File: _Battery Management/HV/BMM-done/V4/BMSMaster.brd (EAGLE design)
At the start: 83.8 x 91.4 mm, 119 parts, among them J1 M2_DF13-2P, J10 IMD, J14 USB_B_RA, J2 M2_DF13-2P, J3 M8S08B-PASK-2(LF)(SN), J5 M16_M_194280016, J6 M2770166, J7 M2770166, J8 M2770166, J9 M2770166, K1 ADJ14024, Q1 IRFR9120TRPBF, Q3 BSS123, U1 SN75HVD08DRMSOP, U10 NC7S14M5X, U11 LTC6820, U12 FT24C64A, U2 NCP1117DT_3.3, U22 NCV7805BDTRKG, U23 NUD3160DMT1G, U3 FT230X, U4 SN74LVC2G241, U5 NC7S14M5X, U6 DSPIC33FJ128GP804, U7 DMG6602SVTQ, U8 LTC6820, U9 MAX823TEUK+T_3.08, Y1 12Mhz

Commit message: Reroute
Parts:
- moved R3 36.9 mm to (77.3, 81.0), flipped to the top
- moved R16 3.45 mm to (35.9, 78.8)
- moved C2 3.32 mm to (33.8, 78.8), turned to 270 degrees
- moved U$1 2.51 mm to (75.6, 81.8), turned to 0 degrees
- moved C1 1.89 mm to (48.9, 72.0)
- moved C18 1.41 mm to (42.9, 73.7)
- moved C19 1.31 mm to (51.2, 74.9)
- moved J11 1.14 mm to (59.2, 82.7)
- moved R29 1.14 mm to (61.8, 78.9)
- moved R30 1.14 mm to (64.2, 78.9)
- moved R31 1.14 mm to (59.3, 78.9)
- moved J12 0.58 mm to (56.1, 91.4)
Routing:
- net SDA: track 68.8 -> 33.5 mm, vias 4 -> 1
- net SCL: track 74.1 -> 39.5 mm, vias 4 -> 1
- net EN1: track 3.93 -> 35.8 mm, vias 0 -> 2
- net +3V3: track 22.9 -> 50.0 mm, vias 1 -> 4
- net CS1: track 4.34 -> 30.0 mm, vias 0 -> 2
- net N$46: track 0.00 -> 6.47 mm, vias 0 -> 1
- net N$45: track 7.06 -> 9.55 mm

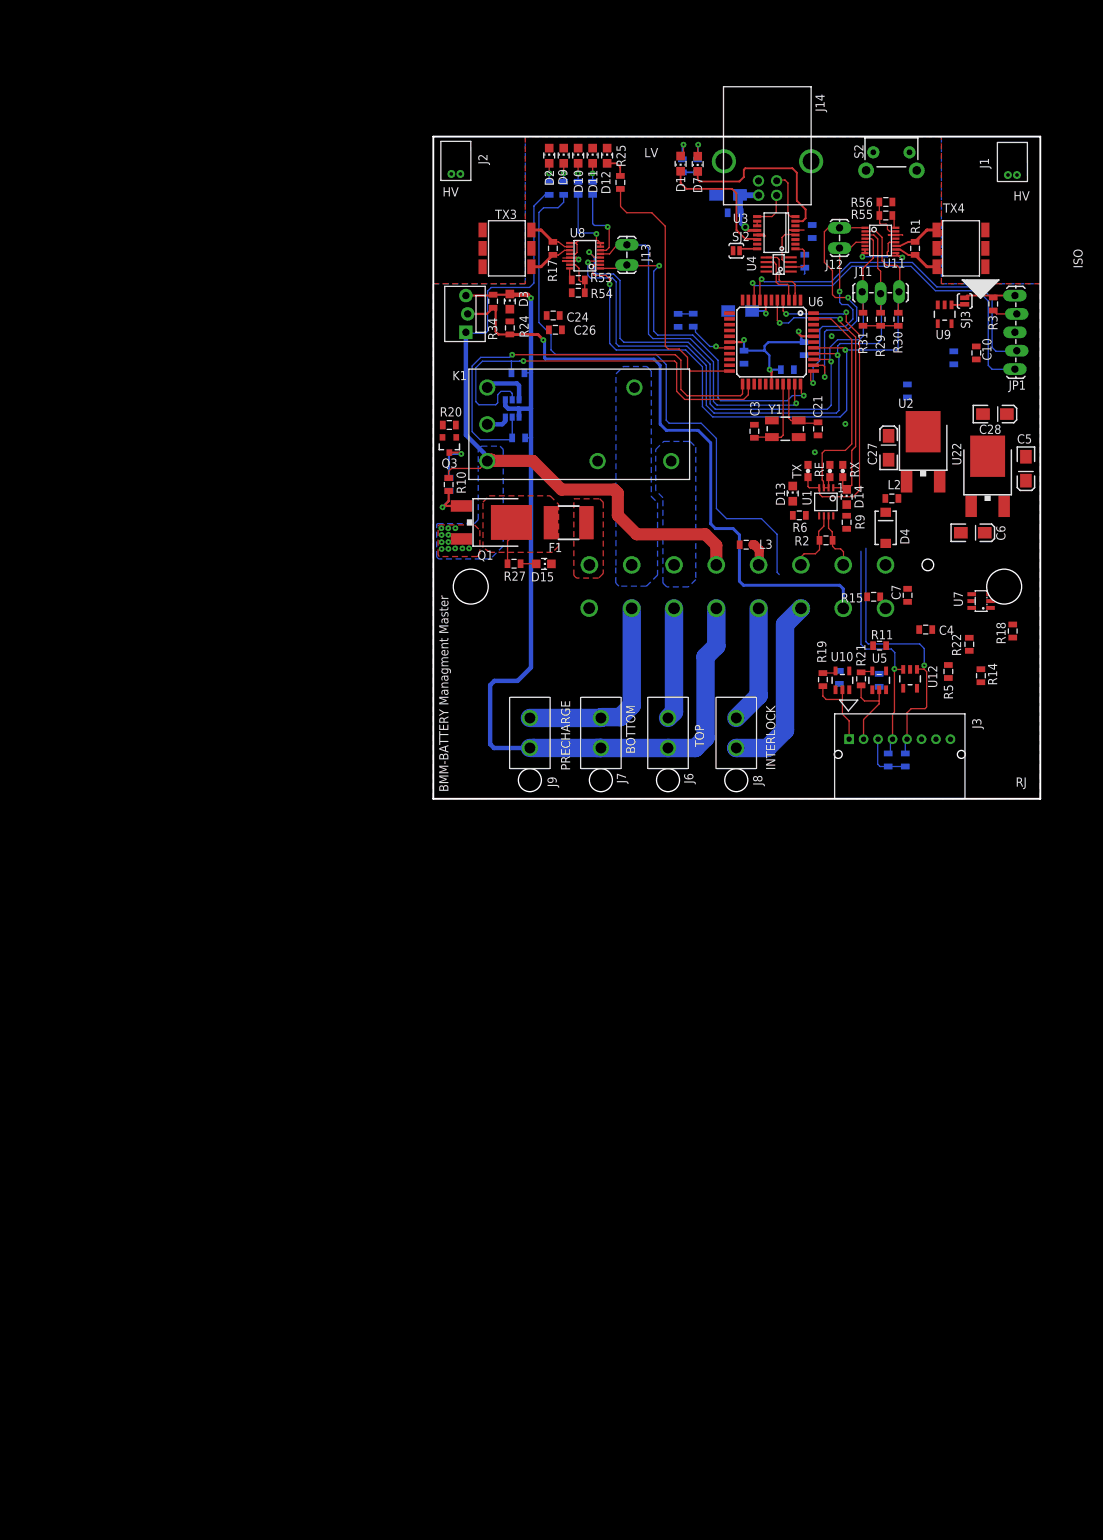
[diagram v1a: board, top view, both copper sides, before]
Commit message: Routing/ changing power supply
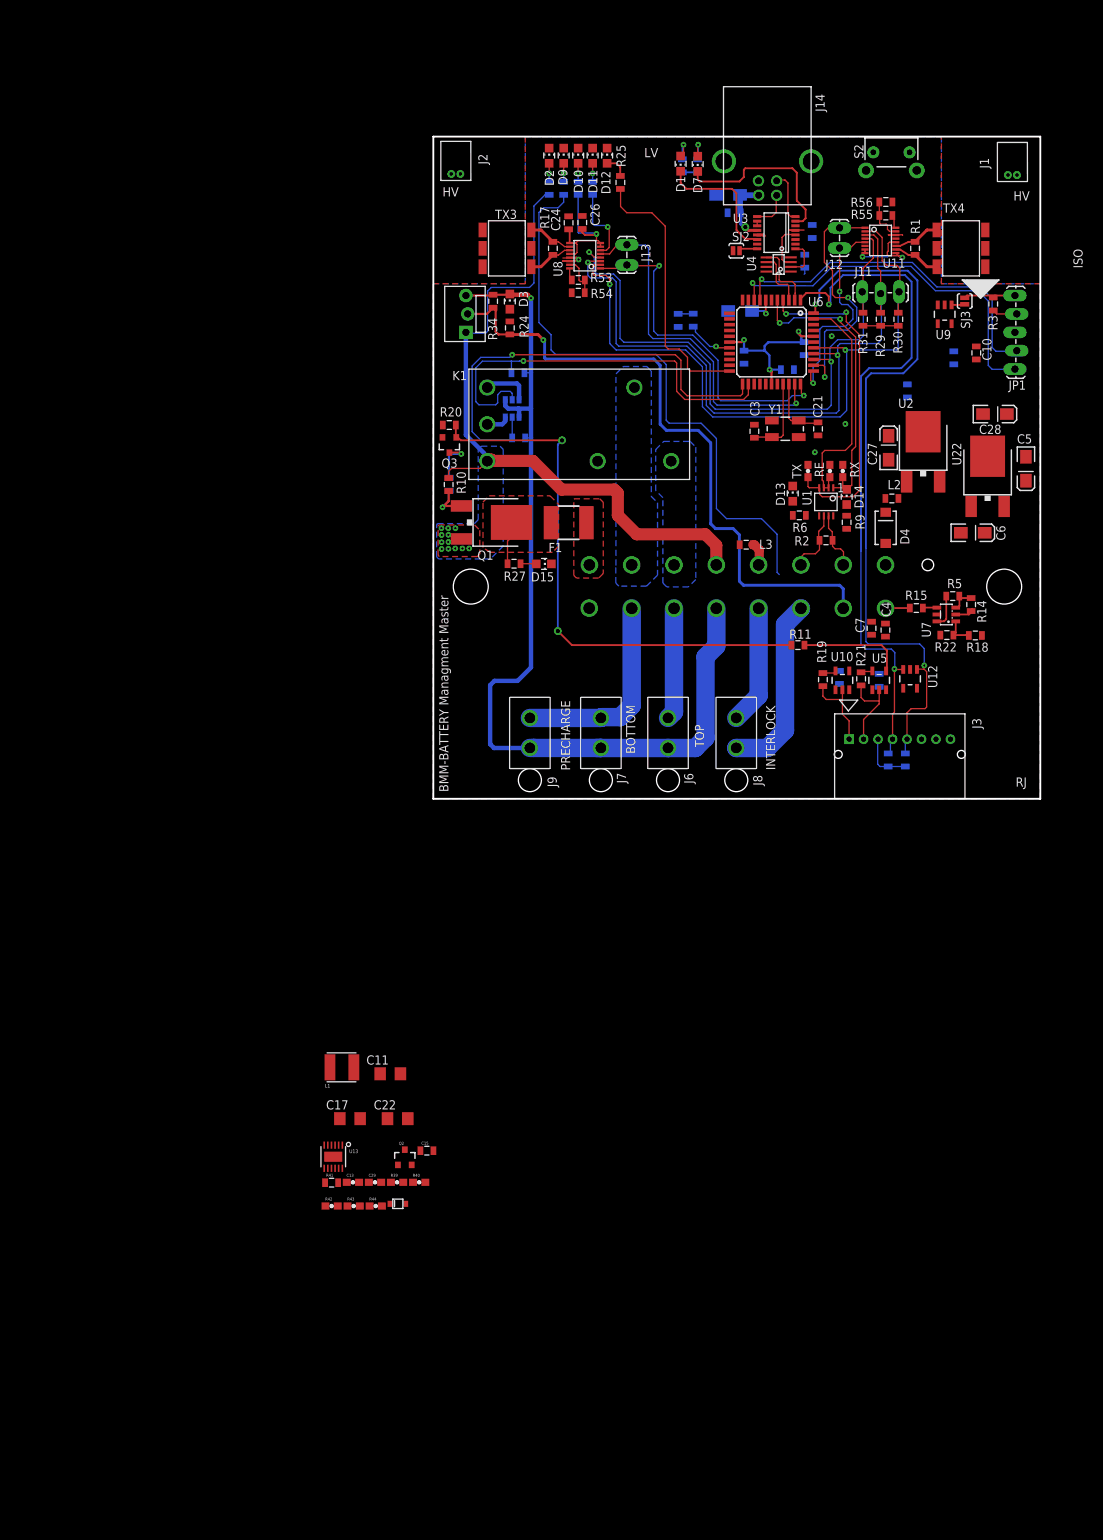
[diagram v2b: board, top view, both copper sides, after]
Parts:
- added C11: 4.7uF, FSAE Electric:1206@1
- added C13: 0.1uF, FSAE Electric:0603
- added C15: 1uF, FSAE Electric:0805
- added C17, C22: 10uF, FSAE Electric:1206@1
- added C29: 100pF, FSAE Electric:0603
- added D5: 22V, FSAE Electric:SOD-323
- added L1: SRN4018-220M, FSAE Electric:SRN4018
- added Q2: 40V 0.2A, FSAE Electric:SOT23
- added R39, R40, R44: 10k, FSAE Electric:0603
- added R41: 91k, FSAE Electric:0805
- added R42: 47k, FSAE Electric:0603
- added R43: 12.4k, FSAE Electric:0603
- added U13: ISL85415-FRZ-T7A, FSAE Electric:DFN-12
- moved C26 15.3 mm to (20.6, 92.3), turned to 90 degrees
- moved C24 13.0 mm to (18.7, 92.2), turned to 90 degrees
- moved R11 11.3 mm to (50.3, 33.9)
- moved R5 10.4 mm to (71.7, 40.7), turned to 0 degrees
- moved R14 9.92 mm to (74.3, 39.5)
- moved C7 6.74 mm to (60.5, 36.2)
- moved R15 6.09 mm to (66.7, 39.0), turned to 0 degrees
- moved C4 5.56 mm to (62.4, 36.0), turned to 270 degrees
- moved R18 5.19 mm to (74.9, 35.3), turned to 180 degrees
- moved U7 5.15 mm to (70.8, 38.2)
- moved R22 3.35 mm to (70.9, 35.3), turned to 0 degrees
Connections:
- new net N$21: D5.P$2, R40.2, R44.1
- new net N$52: Q2.2, R42.2, U13.7
- new net N$53: D5.P$1, R39.1
- new net N$55: C13.1, L1.P$1, U13.5
- new net N$56: C13.2, U13.3
- new net N$57: C15.1, U13.1, U13.11, U13.12, U13.9
- new net N$58: Q2.1, R44.2
- new net N$59: C11.1, Q2.3, R39.2, U13.4
- new net N$66: C29.2, R41.1, R43.2, U13.10
- net +5V: now also C17.1, C22.1, C29.1, L1.P$2, R41.2
- net GND: now also C11.2, C15.2, C17.2, C22.2, R40.1, R42.1, R43.1, U13.13, U13.2, U13.6
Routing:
- net TSAL_EN: track 0.00 -> 76.2 mm, vias 0 -> 2
- net SDA: track 33.5 -> 96.7 mm, vias 1 -> 2
- net SCL: track 39.5 -> 100.9 mm, vias 1 -> 2
- net N$19: track 0.00 -> 15.2 mm
- net +5V: track 32.9 -> 37.5 mm
- net N$40: track 0.00 -> 4.60 mm
- net TSAL_EN1: track 0.00 -> 4.19 mm
- net N$39: track 0.00 -> 3.65 mm
- net CS_OUT: track 0.00 -> 3.59 mm
- net +9V: track 82.3 -> 85.5 mm
- net N$49: track 0.00 -> 1.97 mm

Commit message: Trying to figure out DC/DC converter
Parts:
- removed C11: 4.7uF, FSAE Electric:1206@1
- removed C13: 0.1uF, FSAE Electric:0603
- removed C15: 1uF, FSAE Electric:0805
- removed C17, C22: 10uF, FSAE Electric:1206@1
- removed C27, C28, C5, C6: 10UF, FSAE Electric:EIA3216-16V
- removed C29: 100pF, FSAE Electric:0603
- removed D5: 22V, FSAE Electric:SOD-323
- removed L1: SRN4018-220M, FSAE Electric:SRN4018
- removed Q2: 40V 0.2A, FSAE Electric:SOT23
- removed R39, R40, R44: 10k, FSAE Electric:0603
- removed R41: 91k, FSAE Electric:0805
- removed R42: 47k, FSAE Electric:0603
- removed R43: 12.4k, FSAE Electric:0603
- removed U13: ISL85415-FRZ-T7A, FSAE Electric:DFN-12
- removed U2: NCP1117DT_3.3, FSAE Electric:DPAK
- removed U22: NCV7805BDTRKG, FSAE Electric:DPAK
- moved R34 61.3 mm to (8.20, 20.1), flipped to the bottom, turned to 90 degrees
- moved J10 58.4 mm to (5.36, 21.3), turned to 270 degrees
- moved JP1 37.3 mm to (57.6, 101.7), turned to 180 degrees
- moved R3 33.7 mm to (48.6, 98.7), turned to 0 degrees
- moved U$1 31.6 mm to (47.8, 96.9), turned to 90 degrees
- moved C10 29.5 mm to (55.3, 96.3), turned to 0 degrees
- moved SJ3 28.5 mm to (48.2, 94.7), turned to 180 degrees
- moved C25 25.0 mm to (56.5, 93.3), turned to 180 degrees
- moved U9 24.0 mm to (50.0, 91.9), turned to 270 degrees
- moved D1 20.1 mm to (24.4, 118.0)
- moved R7 20.1 mm to (24.6, 117.7)
- moved D7 20.1 mm to (26.8, 118.0)
- moved R8 20.1 mm to (26.7, 117.7)
- moved R24 19.6 mm to (13.8, 97.0)
- moved D3 19.5 mm to (13.8, 100.6)
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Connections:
- removed net N$21: D5.P$2, R40.2, R44.1
- removed net N$52: Q2.2, R42.2, U13.7
- removed net N$53: D5.P$1, R39.1
- removed net N$55: C13.1, L1.P$1, U13.5
- removed net N$56: C13.2, U13.3
- removed net N$57: C15.1, U13.1, U13.11, U13.12, U13.9
- removed net N$58: Q2.1, R44.2
- removed net N$59: C11.1, Q2.3, R39.2, U13.4
- removed net N$66: C29.2, R41.1, R43.2, U13.10
- new net N$60: L3.1
- net +3V3: no longer C28.A, U2.2
- net +5V: no longer C17.1, C22.1, C27.A, C29.1, L1.P$2, R41.2, U22.3
- net +9V: no longer C5.A, C6.A, U2.3, U22.1
- net GND: no longer C11.2, C15.2, C17.2, C22.2, C27.C, C28.C, C5.C, C6.C, L3.1, R40.1, R42.1, R43.1, U13.13, U13.2, U13.6, U2.1, U22.2
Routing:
- net N$48: track 51.0 -> 0.00 mm, vias 1 -> 0
- net N$47: track 48.5 -> 0.00 mm, vias 1 -> 0
- net VSS: track 132.8 -> 167.7 mm, vias 1 -> 2
- net IMD: track 89.1 -> 123.7 mm, vias 1 -> 4
- net +24V: track 94.7 -> 125.0 mm
- net N$44: track 37.5 -> 11.2 mm
- net N$8: track 24.9 -> 0.00 mm
- net N$10: track 18.4 -> 0.00 mm
- net USB_RX: track 9.41 -> 0.00 mm
- net USB_TX: track 7.87 -> 0.00 mm
- net N$1: track 3.27 -> 0.00 mm
- net +9V: track 85.5 -> 83.0 mm
- net N$42: track 0.00 -> 1.64 mm
- net N$69: track 0.93 -> 0.00 mm
- net N$30: track 2.55 -> 3.38 mm
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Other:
- outline, holes or cut-outs redrawn

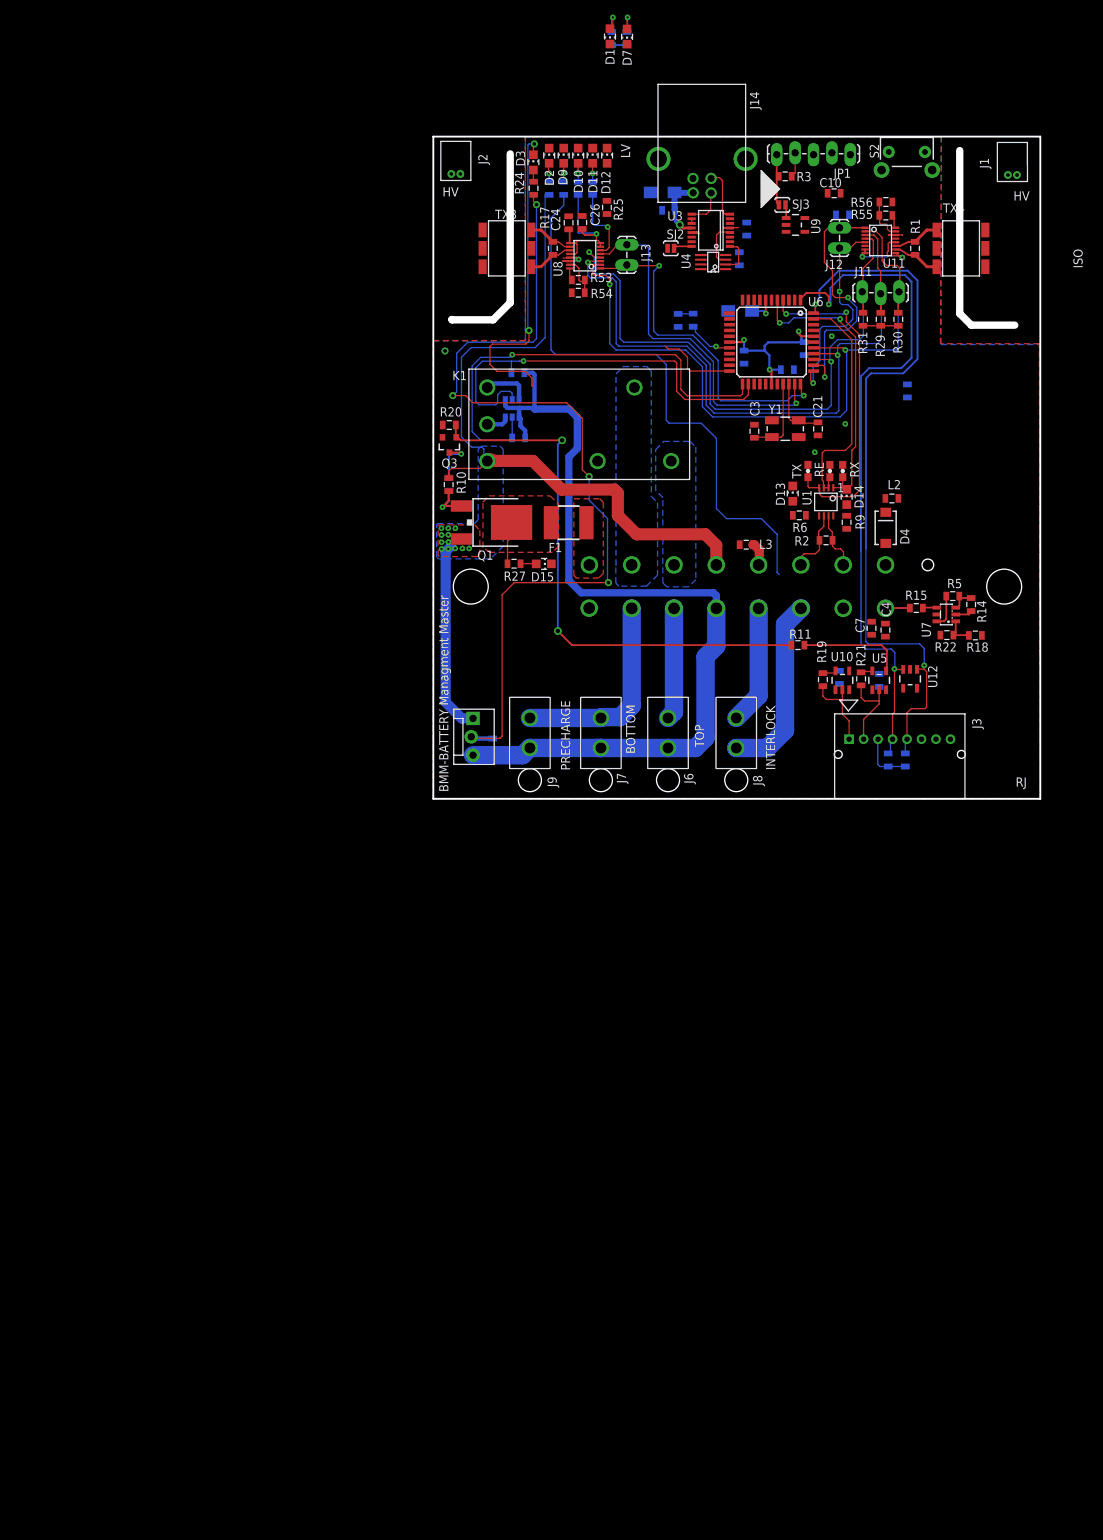
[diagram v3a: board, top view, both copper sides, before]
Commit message: Adding parts and still routing
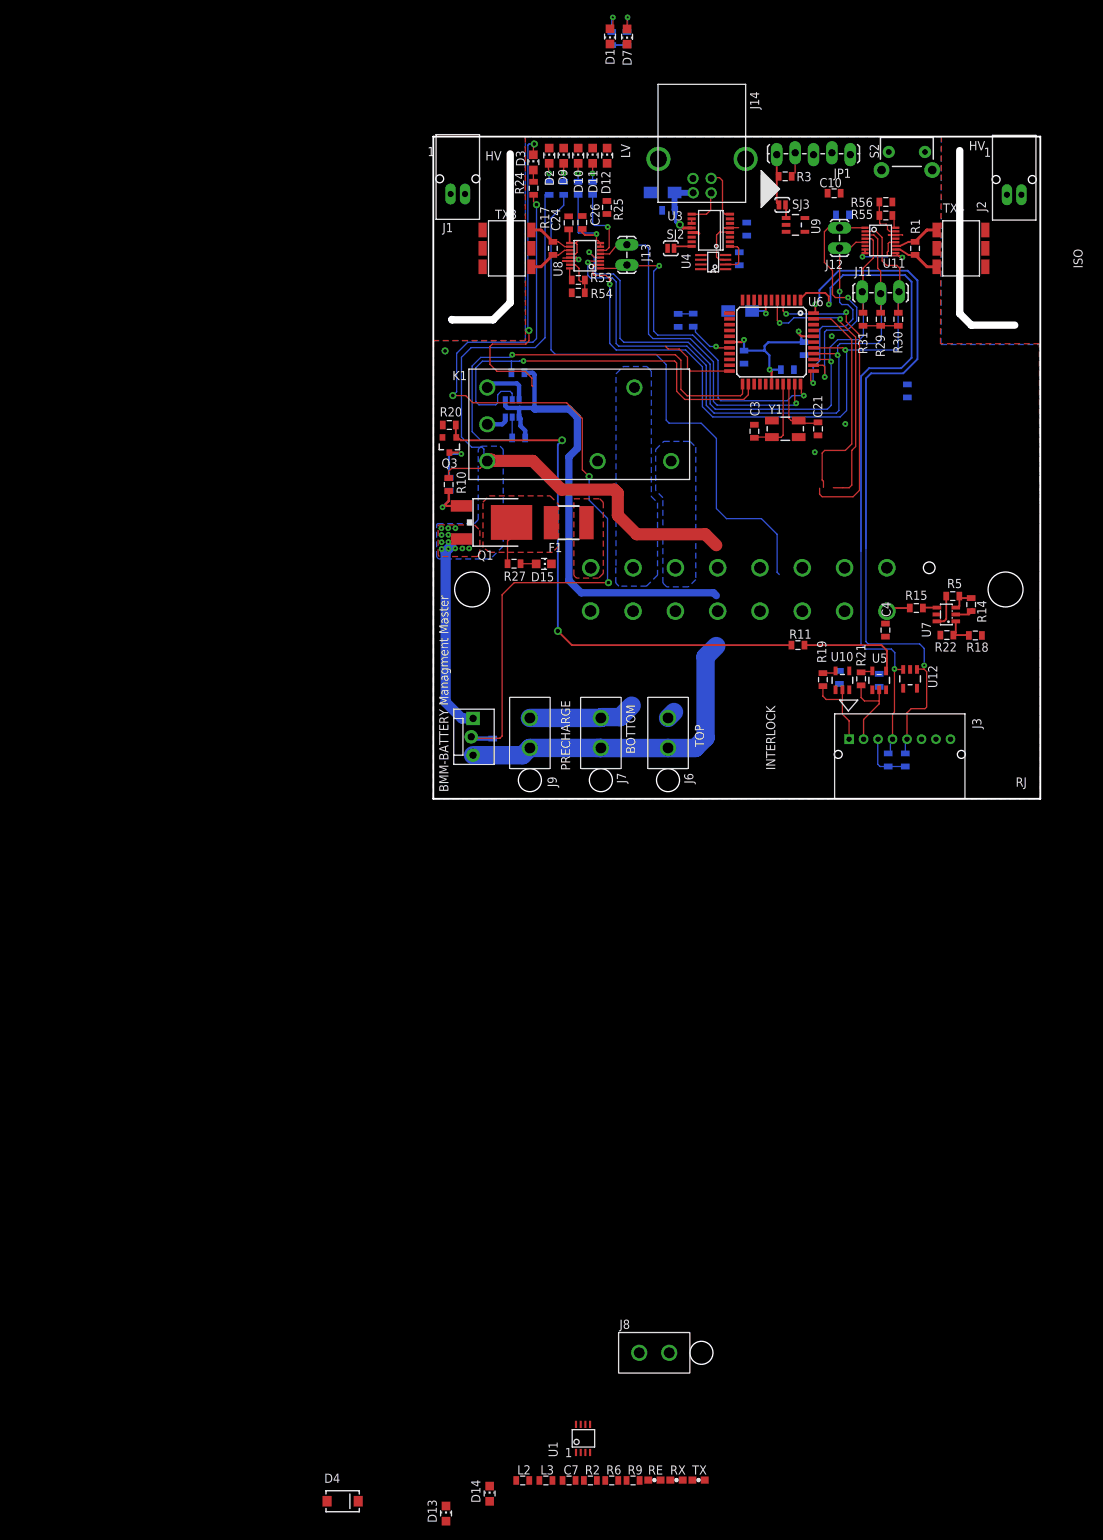
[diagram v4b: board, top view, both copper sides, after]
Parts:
- J1, J2: value M2_DF13-2P -> M2S02B-PASK-2(LF)(SN); device FSAE Electric:DF13-2P -> FSAE Electric:S02B-PASK-2(LF)(SN)
- moved D4 153.9 mm to (-12.5, -84.3), turned to 0 degrees
- moved D13 148.8 mm to (1.75, -86.0)
- moved D14 146.2 mm to (7.77, -83.3)
- moved L2 144.9 mm to (12.3, -81.4), turned to 0 degrees
- moved RE 141.4 mm to (30.5, -81.4), turned to 0 degrees
- moved RX 141.2 mm to (33.6, -81.4), turned to 0 degrees
- moved TX 140.2 mm to (36.6, -81.4), turned to 0 degrees
- moved R6 135.8 mm to (24.6, -81.4)
- moved R9 135.6 mm to (27.6, -81.4), turned to 0 degrees
- moved R2 133.8 mm to (21.7, -81.4), turned to 0 degrees
- moved U1 133.6 mm to (20.7, -75.6), turned to 0 degrees
- moved L3 132.1 mm to (15.5, -81.4)
- moved C7 124.9 mm to (18.7, -81.4), turned to 0 degrees
- moved J8 86.3 mm to (30.5, -63.8), turned to 0 degrees
- moved J2 77.2 mm to (80.2, 96.1)
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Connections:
- removed net N$31: J5.6, K1.C
- removed net N$32: J5.7, K1.NC
- removed net N$59_N: J1.2, TX4.4
- removed net N$61_N: J2.2, TX3.4
- new net N$21: J5.6
- new net N$52: J5.7
- new net N$53: J2.2, TX4.6
- new net N$55: J2.1, TX4.4
- net N$33: now also J1.2, TX3.6; no longer J1.1, TX4.6
- net N$34: now also J1.1, TX3.4; no longer J2.1, TX3.6
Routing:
- net INTERLOCK_IN: track 25.5 -> 0.00 mm
- net INTERLOCK_OUT: track 16.4 -> 0.00 mm
- net TOP_AIR: track 15.5 -> 1.17 mm
- net PRE_CRG-B_AIR: track 28.2 -> 14.8 mm
- net N$24: track 9.14 -> 0.00 mm
- net N$23: track 8.09 -> 0.00 mm
- net VSS: track 167.7 -> 160.8 mm
- net TX2: track 47.3 -> 42.7 mm
- net RE: track 34.3 -> 30.3 mm
- net RX2: track 42.2 -> 38.8 mm
- net N$88: track 3.32 -> 0.00 mm
- net +24V: track 125.0 -> 122.2 mm
- net +3V3: track 50.0 -> 49.4 mm
